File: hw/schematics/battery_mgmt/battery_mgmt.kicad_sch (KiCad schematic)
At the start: 21 parts, among them J5 Battery Connector, U1 LTC2942, U2 MAX77751CEFG+

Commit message: 
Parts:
- removed D?: LED_Filled, LED_SMD:LED_0402_1005Metric, symbol Device:LED_Filled
- removed J5: Battery Connector, 0:JST_ACH_BM03B-ACHSS-GAN-ETF, symbol 4ms_Connector:Conn_01x03
- removed Q? (x2): NTND31015NZTAG, 0:NTND31015NZTAG, symbol Device:Q_Dual_PMOS_S1G1D2S2G2D1
- removed R?: 470${R}, Resistor_SMD:R_0201_0603Metric, symbol Device:R
- removed R? (x3): 100${kR}, Resistor_SMD:R_0201_0603Metric, symbol Device:R
- removed R? (x3): R, Resistor_SMD:R_0201_0603Metric, symbol Device:R
- removed R?: 1M${R}, Resistor_SMD:R_0201_0603Metric, symbol Device:R
- removed R?: RITOPOFF, Resistor_SMD:R_0201_0603Metric, symbol Device:R
- removed U? (x2): MAX9027EBT+T, 0:MAX9027EBT-T, symbol 0.Project:MAX9027EBT+T
- added J?: Conn_01x02, symbol Connector_Generic:Conn_01x02
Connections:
- net BATT+: now also J?.1 (Pin_1)
- net BATT-: now also J?.2 (Pin_2)
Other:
- note removed: "INOKB control"
- note removed: "Temperature Detection"
- moved on the sheet: U2A, U2B

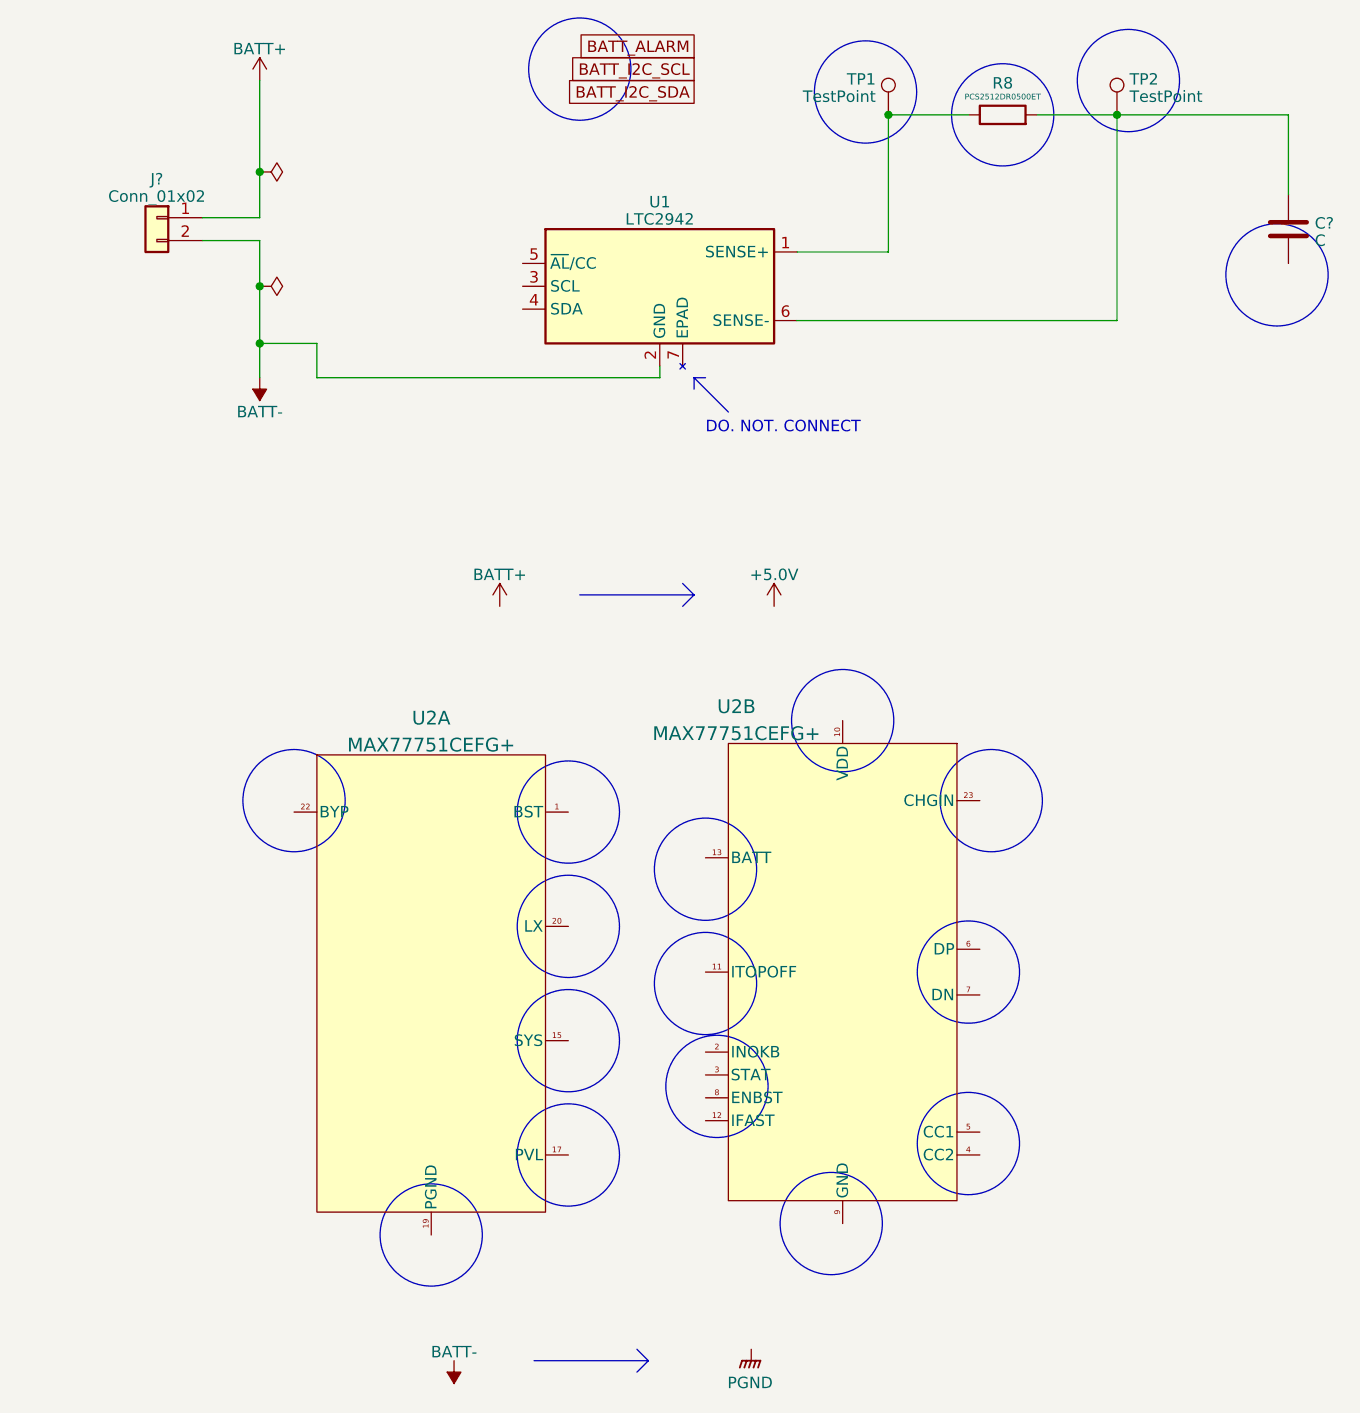
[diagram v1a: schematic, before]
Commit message: 
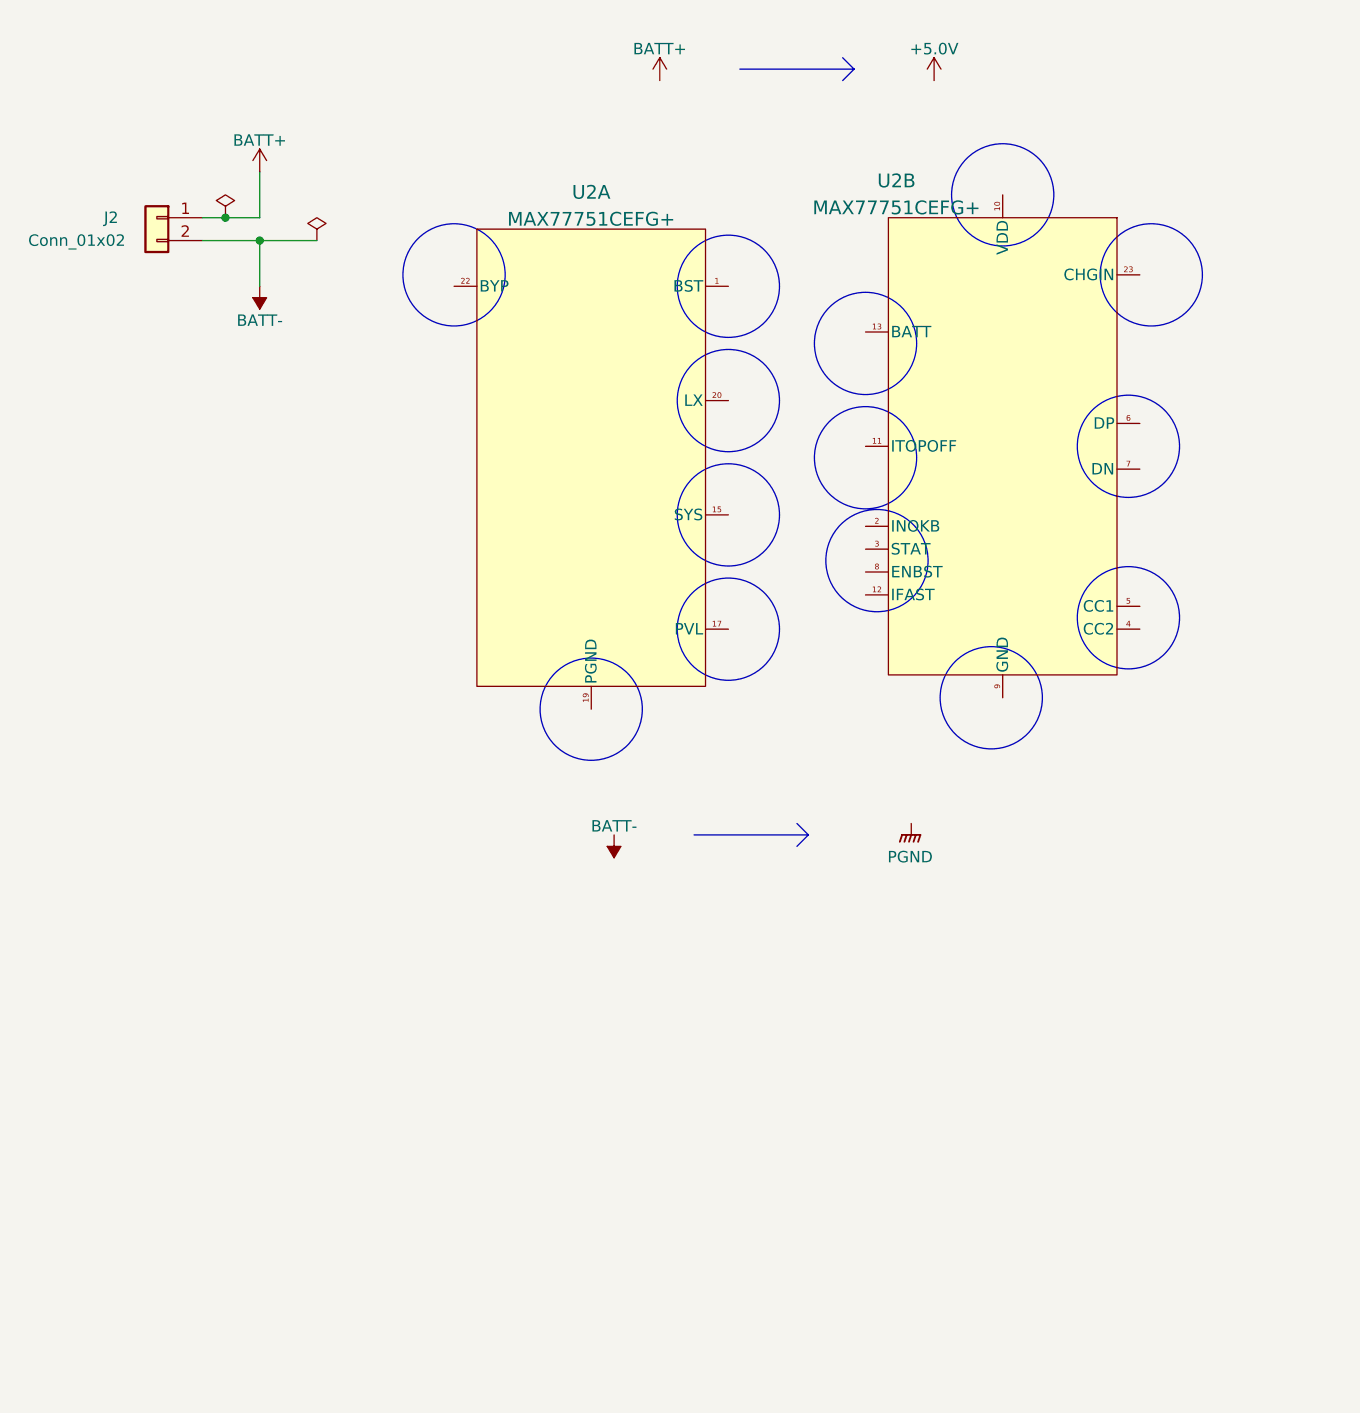
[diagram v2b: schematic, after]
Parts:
- removed C?: C, symbol Device:C
- removed R8: PCS2512DR0500ET, 0:PCS2512DR0500ET, symbol 0.Project:PCS2512DR0500ET
- removed TP1, TP2: TestPoint, symbol 4ms_Connector:TestPoint
- removed U1: LTC2942, 0:LTC2942, symbol 0.Project:LTC2942
- J2: renamed from J?; footprint (none) -> 0:DF57H-2P-1-2V-21
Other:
- note removed: "DO. NOT. CONNECT"
- moved on the sheet: U2A, U2B
